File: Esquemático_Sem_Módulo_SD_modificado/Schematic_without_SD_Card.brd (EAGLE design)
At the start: 64.7 x 48.2 mm, 8 parts

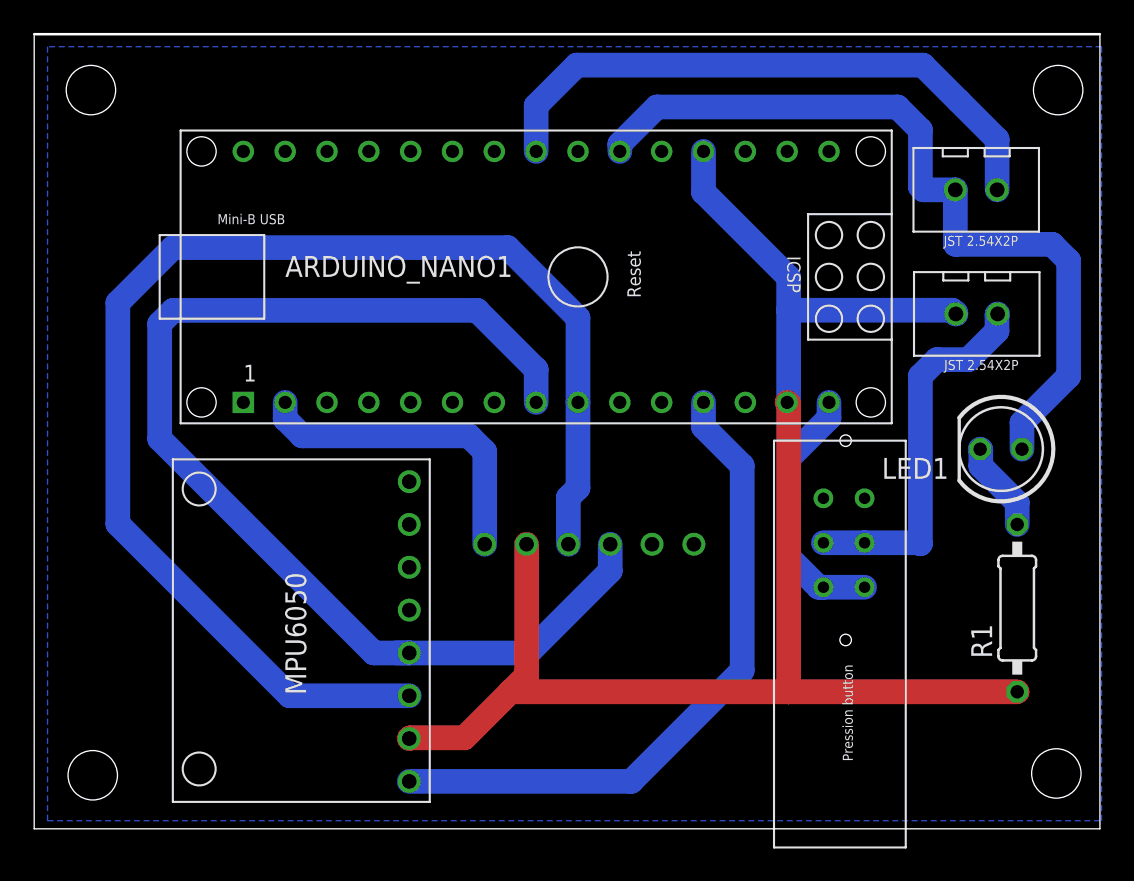
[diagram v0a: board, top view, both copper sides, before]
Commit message: Tamanho dos pads modificado (10mil - 30mil - 80%)
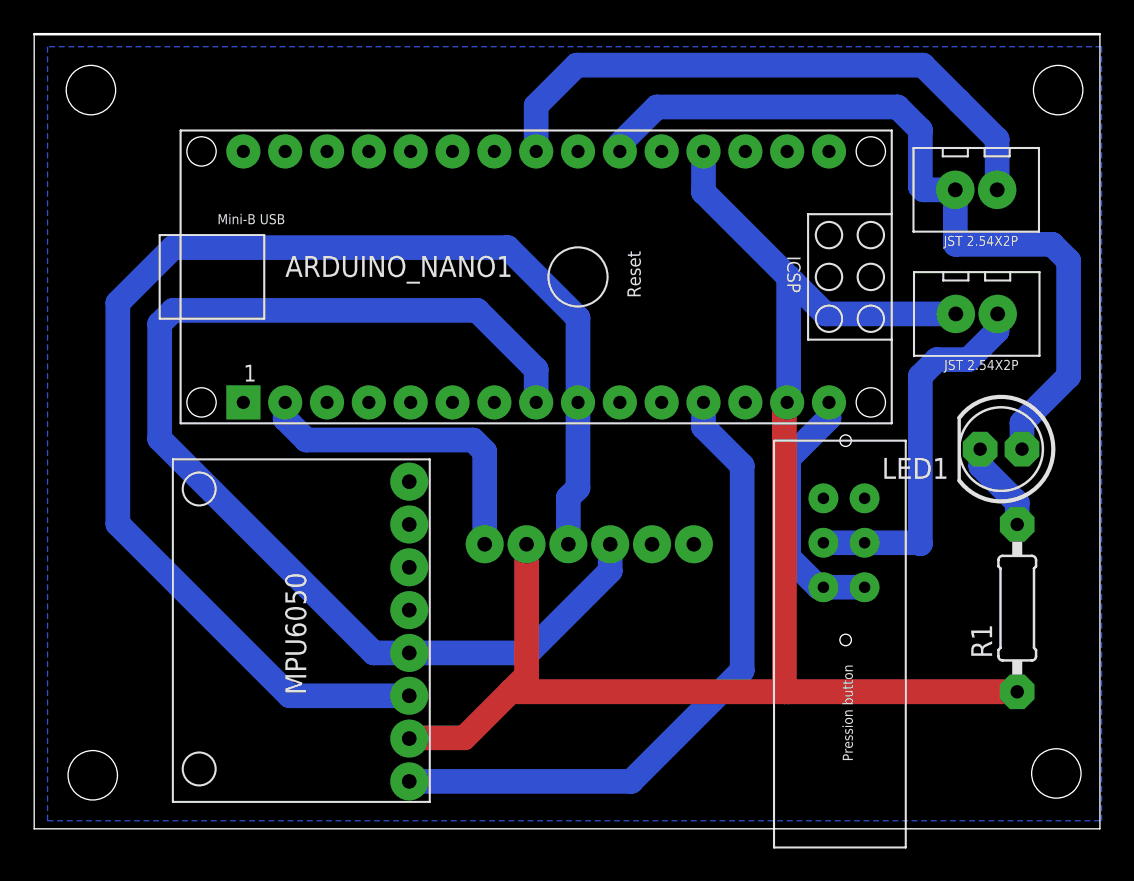
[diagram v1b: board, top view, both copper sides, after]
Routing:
- net GND: track 92.9 -> 93.7 mm
- net N$3: track 70.9 -> 70.1 mm
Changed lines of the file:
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@@
 <param name="msMicroVia" value="9.99mm"/>
 <param name="msBlindViaRatio" value="0.5"/>
-<param name="rvPadTop" value="0.25"/>
+<param name="rvPadTop" value="0.8"/>
 <param name="rvPadInner" value="0.25"/>
-<param name="rvPadBottom" value="0.25"/>
+<param name="rvPadBottom" value="0.8"/>
 <param name="rvViaOuter" value="0.25"/>
 <param name="rvViaInner" value="0.25"/>
@@
 <param name="rvMicroViaInner" value="0.25"/>
 <param name="rlMinPadTop" value="10mil"/>
-<param name="rlMaxPadTop" value="20mil"/>
+<param name="rlMaxPadTop" value="30mil"/>
 <param name="rlMinPadInner" value="10mil"/>
 <param name="rlMaxPadInner" value="20mil"/>
 <param name="rlMinPadBottom" value="10mil"/>
-<param name="rlMaxPadBottom" value="20mil"/>
+<param name="rlMaxPadBottom" value="30mil"/>
 <param name="rlMinViaOuter" value="8mil"/>
 <param name="rlMaxViaOuter" value="20mil"/>
@@
 <contactref element="ARDUINO_NANO1" pad="2"/>
 <contactref element="U$1" pad="VCC"/>
-<wire x1="22.59" y1="40.37" x2="23.48" y2="39.48" width="1.5" layer="16"/>
-<wire x1="22.59" y1="40.37" x2="12.462" y2="40.37" width="1.5" layer="16"/>
-<wire x1="12.462" y1="40.37" x2="11.43" y2="41.402" width="1.5" layer="16"/>
+<wire x1="22.844" y1="40.116" x2="23.5455" y2="39.4145" width="1.5" layer="16"/>
+<wire x1="22.844" y1="40.116" x2="12.716" y2="40.116" width="1.5" layer="16"/>
+<wire x1="12.716" y1="40.116" x2="11.43" y2="41.402" width="1.5" layer="16"/>
 <wire x1="11.43" y1="41.402" x2="11.43" y2="42.402" width="1.5" layer="16"/>
 <wire x1="23.5455" y1="33.79" x2="23.5455" y2="39.4145" width="1.5" layer="16"/>
-<wire x1="23.5455" y1="39.4145" x2="23.48" y2="39.48" width="1.5" layer="16"/>
 </signal>
 <signal name="N$3">
@@
 <wire x1="26.67" y1="44.402" x2="23.082" y2="47.99" width="1.5" layer="16"/>
 <wire x1="23.082" y1="47.99" x2="4.62815625" y2="47.99" width="1.5" layer="16"/>
-<wire x1="18.1795" y1="27.1905" x2="18.9635" y2="27.1905" width="1.5" layer="16"/>
-<wire x1="18.9635" y1="27.1905" x2="16.8095" y2="27.1905" width="1.5" layer="16"/>
-<wire x1="16.8095" y1="27.1905" x2="3.81" y2="40.19" width="1.5" layer="16"/>
+<wire x1="3.81" y1="40.19" x2="16.8095" y2="27.1905" width="1.5" layer="16"/>
 <wire x1="31.1655" y1="32.1655" x2="31.1655" y2="33.79" width="1.5" layer="16"/>
 <wire x1="18.9635" y1="27.1905" x2="26.1905" y2="27.1905" width="1.5" layer="16"/>
 <wire x1="26.1905" y1="27.1905" x2="31.1655" y2="32.1655" width="1.5" layer="16"/>
+<wire x1="16.8095" y1="27.1905" x2="18.9635" y2="27.1905" width="1.5" layer="16"/>
 </signal>
 <signal name="N$2">
@@
 <contactref element="U$6" pad="2"/>
 <contactref element="ARDUINO_NANO1" pad="19"/>
-<wire x1="52.152" y1="47.848" x2="52.152" y2="47.774" width="1.5" layer="16"/>
 <wire x1="36.83" y1="57.642" x2="36.83" y2="55.17" width="1.5" layer="16"/>
 <wire x1="36.83" y1="55.17" x2="42" y2="50" width="1.5" layer="16"/>
-<wire x1="42" y1="50" x2="42" y2="48" width="1.5" layer="16"/>
-<wire x1="42" y1="48" x2="42" y2="42.492" width="1.5" layer="16"/>
+<wire x1="42" y1="50" x2="42" y2="42.492" width="1.5" layer="16"/>
 <wire x1="42" y1="42.492" x2="41.91" y2="42.402" width="1.5" layer="16"/>
-<wire x1="52.152" y1="47.774" x2="51.926" y2="48" width="1.5" layer="16"/>
-<wire x1="51.926" y1="48" x2="42" y2="48" width="1.5" layer="16"/>
 <wire x1="19.006" y1="22.033" x2="22.30443125" y2="22.033" width="1.5" layer="1"/>
 <wire x1="19.006" y1="22.033" x2="18.9635" y2="21.9905" width="1.5" layer="1"/>
@@
 <wire x1="25.17" y1="24.83" x2="25.135715625" y2="24.864284375" width="1.5" layer="1"/>
 <wire x1="55.88" y1="24.83" x2="42" y2="24.83" width="1.5" layer="1"/>
-<wire x1="42" y1="24.83" x2="25.17" y2="24.83" width="1.5" layer="1"/>
+<wire x1="42" y1="24.83" x2="41.746" y2="24.83" width="1.5" layer="1"/>
+<wire x1="41.746" y1="24.83" x2="25.17" y2="24.83" width="1.5" layer="1"/>
 <wire x1="41.91" y1="24.92" x2="42" y2="24.83" width="1.5" layer="1"/>
-<wire x1="41.91" y1="42.402" x2="42" y2="42.312" width="1.5" layer="1"/>
-<wire x1="42" y1="42.312" x2="42" y2="24.83" width="1.5" layer="1"/>
+<wire x1="41.91" y1="42.402" x2="41.746" y2="42.238" width="1.5" layer="1"/>
+<wire x1="41.746" y1="42.238" x2="41.746" y2="24.83" width="1.5" layer="1"/>
+<wire x1="52.152" y1="47.774" x2="44.226" y2="47.774" width="1.5" layer="16"/>
+<wire x1="44.226" y1="47.774" x2="42" y2="50" width="1.5" layer="16"/>
 </signal>
 <signal name="N$5">

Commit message: adjusts
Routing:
- net N$4: track 15.8 -> 16.4 mm
- net N$11: track 49.1 -> 49.6 mm
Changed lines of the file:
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@@
 <contactref element="ARDUINO_NANO1" pad="2"/>
 <contactref element="U$1" pad="VCC"/>
-<wire x1="22.844" y1="40.116" x2="23.5455" y2="39.4145" width="1.5" layer="16"/>
-<wire x1="22.844" y1="40.116" x2="12.716" y2="40.116" width="1.5" layer="16"/>
-<wire x1="12.716" y1="40.116" x2="11.43" y2="41.402" width="1.5" layer="16"/>
+<wire x1="22.971" y1="39.989" x2="23.5455" y2="39.4145" width="1.5" layer="16"/>
+<wire x1="22.971" y1="39.989" x2="12.843" y2="39.989" width="1.5" layer="16"/>
+<wire x1="12.843" y1="39.989" x2="11.43" y2="41.402" width="1.5" layer="16"/>
 <wire x1="11.43" y1="41.402" x2="11.43" y2="42.402" width="1.5" layer="16"/>
 <wire x1="23.5455" y1="33.79" x2="23.5455" y2="39.4145" width="1.5" layer="16"/>
@@
 <contactref element="ARDUINO_NANO1" pad="21"/>
 <contactref element="LED1" pad="A"/>
-<wire x1="48.609" y1="60.341" x2="34" y2="60.341" width="1.5" layer="16"/>
+<wire x1="48.609" y1="60.341" x2="33.111" y2="60.341" width="1.5" layer="16"/>
 <wire x1="48.609" y1="60.341" x2="50" y2="58.95" width="1.5" layer="16"/>
 <wire x1="50" y1="58.95" x2="50" y2="55.499" width="1.5" layer="16"/>
@@
 <wire x1="56.168" y1="41.168" x2="56.168" y2="39.565" width="1.5" layer="16"/>
 <wire x1="59" y1="44" x2="56.168" y2="41.168" width="1.5" layer="16"/>
-<wire x1="34" y1="60.341" x2="31.75" y2="58.091" width="1.5" layer="16"/>
-<wire x1="31.75" y1="58.091" x2="31.75" y2="57.642" width="1.5" layer="16"/>
+<wire x1="33.111" y1="60.341" x2="31.75" y2="58.98" width="1.5" layer="16"/>
+<wire x1="31.75" y1="58.98" x2="31.75" y2="57.642" width="1.5" layer="16"/>
 <wire x1="52.12" y1="55.31" x2="50.189" y2="55.31" width="1.5" layer="16"/>
 <wire x1="50.189" y1="55.31" x2="50" y2="55.499" width="1.5" layer="16"/>
@@
 <contactref element="U$3" pad="PR2"/>
 <wire x1="54.692" y1="47.774" x2="54.652" y2="47.734" width="1.5" layer="16"/>
-<wire x1="54.652" y1="47.734" x2="54.652" y2="46.7384625" width="1.5" layer="16"/>
-<wire x1="54.652" y1="46.7384625" x2="52.9135375" y2="45" width="1.5" layer="16"/>
-<wire x1="52.9135375" y1="45" x2="51" y2="45" width="1.5" layer="16"/>
+<wire x1="54.652" y1="47.734" x2="54.652" y2="46.4844625" width="1.5" layer="16"/>
+<wire x1="54.652" y1="46.4844625" x2="53.1675375" y2="45" width="1.5" layer="16"/>
+<wire x1="53.1675375" y1="45" x2="51" y2="45" width="1.5" layer="16"/>
 <wire x1="51" y1="45" x2="50" y2="44" width="1.5" layer="16"/>
 <wire x1="50" y1="44" x2="50" y2="33.82" width="1.5" layer="16"/>
@@
 <contactref element="U$3" pad="PR3"/>
 <wire x1="46.6114" y1="31.178796875" x2="44.1114" y2="31.178796875" width="1.5" layer="16"/>
-<wire x1="44.45" y1="42.402" x2="44.45" y2="41.45" width="1.5" layer="16"/>
-<wire x1="42" y1="33" x2="43.821203125" y2="31.178796875" width="1.5" layer="16"/>
-<wire x1="43.821203125" y1="31.178796875" x2="44.1114" y2="31.178796875" width="1.5" layer="16"/>
-<wire x1="44.45" y1="41.45" x2="42" y2="39" width="1.5" layer="16"/>
-<wire x1="42" y1="39" x2="42" y2="33" width="1.5" layer="16"/>
+<wire x1="44.45" y1="42.402" x2="44.45" y2="41.323" width="1.5" layer="16"/>
+<wire x1="41.746" y1="32.492" x2="43.059203125" y2="31.178796875" width="1.5" layer="16"/>
+<wire x1="43.059203125" y1="31.178796875" x2="44.1114" y2="31.178796875" width="1.5" layer="16"/>
+<wire x1="44.45" y1="41.323" x2="41.746" y2="38.619" width="1.5" layer="16"/>
+<wire x1="41.746" y1="38.619" x2="41.746" y2="32.492" width="1.5" layer="16"/>
 </signal>
 </signals>
